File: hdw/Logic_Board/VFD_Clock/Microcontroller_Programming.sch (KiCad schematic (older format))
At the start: 11 parts

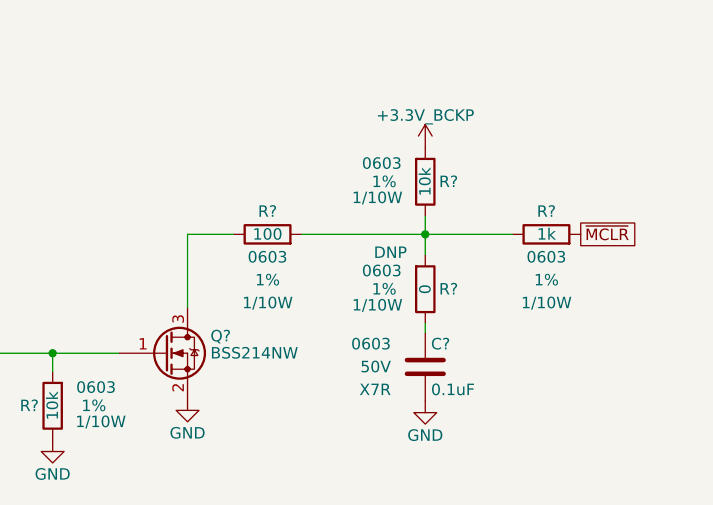
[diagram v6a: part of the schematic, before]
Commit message: Started IV-6 display board, continued logic board development
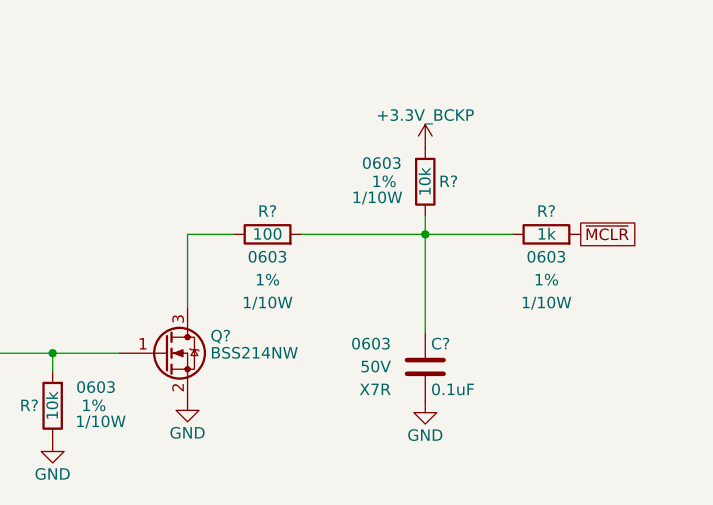
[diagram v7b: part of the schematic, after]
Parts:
- removed R?: 0, Resistors_SMD:R_0603, symbol Custom_Library:R_Custom
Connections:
- net at R?.1, R?.2, R?.2: now also C?.1
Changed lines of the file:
@@
 $EndComp
-$Comp
-L Custom_Library:R_Custom R?
-U 1 1 5BC15CB4
-P 7550 2490
-AR Path="/5BAAE1F3/5BC15CB4" Ref="R?"  Part="1"
-AR Path="/5BAAE1DC/5BC15CB4" Ref="R?"  Part="1"
-AR Path="/5BAAE16C/5BC15CB4" Ref="R?"  Part="1"
-AR Path="/5C1D5CB6/5BC15CB4" Ref="R?"  Part="1"
-AR Path="/5CB0BC26/5BC15CB4" Ref="R?"  Part="1"
-F 0 "R?" H 7490 2490 50  0000 R CNN
-F 1 "0" V 7550 2490 50  0000 C CNN
-F 2 "Resistors_SMD:R_0603" H 7550 2490 50  0001 C CNN
-F 3 "" H 7550 2490 50  0001 C CNN
-F 4 "DNP" H 7630 2650 50  0000 L CNN "Config"
-F 5 "311-0.0GRCT-ND" H 7850 2890 60  0001 C CNN "Digi-Key PN"
-F 6 "0603" H 7740 2570 50  0000 C CNN "display_footprint"
-F 7 "1%" H 7730 2490 50  0000 C CNN "Tolerance"
-F 8 "1/10W" H 7760 2420 50  0000 C CNN "Wattage"
-	1    7550 2490
-	-1   0    0    -1
-$EndComp
-Wire Wire Line
-	7550 2640 7550 2680
 $Comp
 L power:GND #PWR?
@@
 	7930 2250 7550 2250
 Connection ~ 7550 2250
-Wire Wire Line
-	7550 2250 7550 2340
 Text GLabel 8230 2250 2    50   UnSpc ~ 0
 ~MCLR
@@
 	1    0    0    -1
 $EndComp
+Wire Wire Line
+	7550 2680 7550 2250
 $EndSCHEMATC
